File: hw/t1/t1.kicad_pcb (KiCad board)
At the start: 4 copper layers, 58 x 11.8 mm, 17 parts, among them J1 SFP_Module_Edge, J2 H-MTD PCB header (Rosenberger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, U1 DP83TG720S-Q1 / DP83TC812S-Q1, U2 STM32G031F6P6 (I2C slave: EEP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, U3 TPS62A01 3V3->1V0, Y1 25 MHz

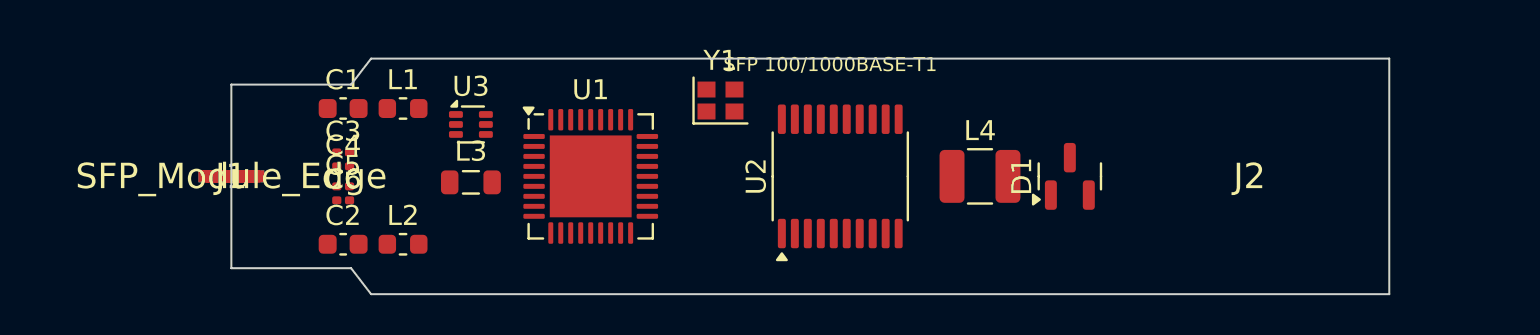
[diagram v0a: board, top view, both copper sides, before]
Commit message: T1 module: schematic, routed 4-layer PCB, fab outputs, controller firmware
One netlist in make_t1.py drives both the schematic and the PCB pad nets;
the schematic's exported netlist matches it pin for pin (175 pins), and
eeschema's ERC is clean. Every block is from its datasheet: DP83TG720S
pins, straps, MDI network and decoupling; the DP83TC812S loadout differs
only in leaving FB3 off; TPS62821 1.0 V buck.

Routed by Freerouting 1.9.0 with In1 GND / In2 3V3 planes, outer GND
pours added after import, no pour among the gold fingers. KiCad DRC:
0 violations, 0 unconnected.

Firmware (STM32G031, 1.7 KB): A0h EEPROM emulation, I2C-to-MDIO bridge at
0x56 in the mdio-i2c protocol, TX_DISABLE holds the PHY in reset, RX_LOS
follows the link.

Not orderable yet: the H-MTD footprint is a placeholder and the SGMII
widths wait on the fab's stackup.
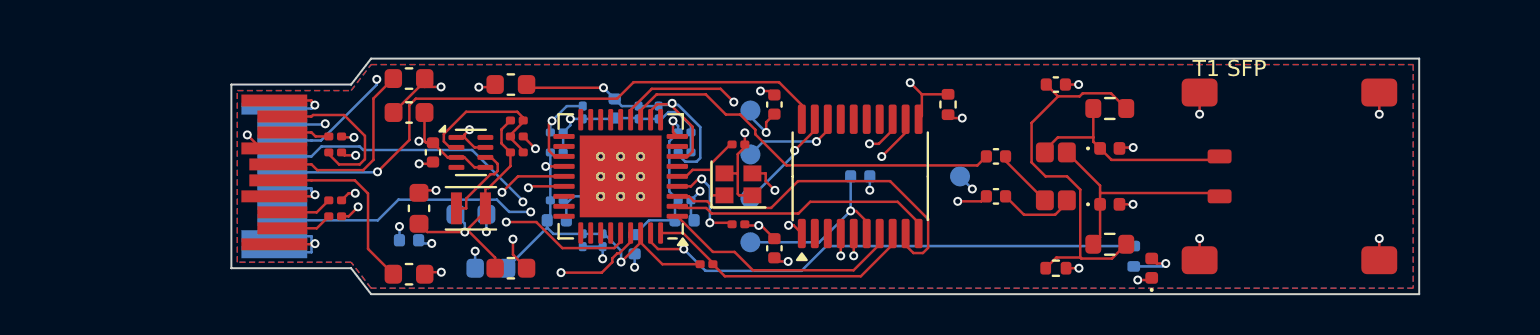
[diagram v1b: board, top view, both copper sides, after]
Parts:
- removed L3: 1uH, L_0805_2012Metric
- removed L4: CMC (ACT1210 class), L_1210_3225Metric
- added C10: 100nF, Capacitor_SMD:C_0201_0603Metric, B.Cu at (122.7, 98.8)
- added C11: 10nF, Capacitor_SMD:C_0201_0603Metric, B.Cu at (117.6, 103.2)
- added C12: 100nF, Capacitor_SMD:C_0201_0603Metric, B.Cu at (118.6, 103.2)
- added C13: 10nF, Capacitor_SMD:C_0201_0603Metric, B.Cu at (116.3, 98.8)
- added C14: 100nF, Capacitor_SMD:C_0201_0603Metric, B.Cu at (116.3, 101.2)
- added C15: 2.2uF, Capacitor_SMD:C_0402_1005Metric, B.Cu at (116.3, 102.2)
- added C16: 10nF, Capacitor_SMD:C_0201_0603Metric, B.Cu at (122.7, 97.8)
- added C17: 100nF, Capacitor_SMD:C_0201_0603Metric, B.Cu at (122.7, 101.2)
- added C18: 2.2uF, Capacitor_SMD:C_0402_1005Metric, B.Cu at (122.7, 102.2)
- added C19: 10nF, Capacitor_SMD:C_0201_0603Metric, B.Cu at (116.3, 97.8)
- added C20: 100nF, Capacitor_SMD:C_0201_0603Metric, B.Cu at (117.6, 96.8)
- added C21: 2.2uF, Capacitor_SMD:C_0402_1005Metric, B.Cu at (120.2, 103.4)
- added C24: 12pF, Capacitor_SMD:C_0201_0603Metric, F.Cu at (125.4, 98.4)
- added C25: 12pF, Capacitor_SMD:C_0201_0603Metric, F.Cu at (125.4, 102.4)
- added C26: 4.7uF, Capacitor_SMD:C_0402_1005Metric, F.Cu at (110.1, 98.8)
- added C27: 10uF, Capacitor_SMD:C_0603_1608Metric, F.Cu at (109.4, 101.6)
- added C28: 10uF, Capacitor_SMD:C_0603_1608Metric, B.Cu at (112.0, 101.9)
- added C29: 120pF, Capacitor_SMD:C_0201_0603Metric, F.Cu at (114.3, 98.8)
- added C30: 100nF, Capacitor_SMD:C_0402_1005Metric, F.Cu at (127.2, 96.4)
- added C31: 1uF, Capacitor_SMD:C_0402_1005Metric, F.Cu at (127.2, 103.6)
- added C32: 100nF, Capacitor_SMD:C_0402_1005Metric, B.Cu at (131.5, 100.0)
- added C33: 100nF 1%, Capacitor_SMD:C_0402_1005Metric, F.Cu at (138.3, 99.0)
- added C34: 100nF 1%, Capacitor_SMD:C_0402_1005Metric, F.Cu at (138.3, 101.0)
- added C35: 4.7nF, Capacitor_SMD:C_0402_1005Metric, F.Cu at (141.3, 95.4)
- added C7: 10nF, Capacitor_SMD:C_0201_0603Metric, B.Cu at (121.4, 96.8)
- added C8: 100nF, Capacitor_SMD:C_0201_0603Metric, B.Cu at (120.4, 96.8)
- added C9: 2.2uF, Capacitor_SMD:C_0402_1005Metric, B.Cu at (119.2, 96.6)
- added D2: ESD (DNP), Diode_SMD:D_0402_1005Metric, F.Cu at (144.0, 98.6)
- added D3: ESD (DNP), Diode_SMD:D_0402_1005Metric, F.Cu at (144.0, 101.4)
- added FB1: BLM18KG601SH1, Inductor_SMD:L_0603_1608Metric, F.Cu at (108.9, 95.1)
- added FB2: BLM18KG601SH1, Inductor_SMD:L_0603_1608Metric, F.Cu at (108.9, 104.9)
- added FB3: BLM18KG601SH1 (DNP for DP83TC812), Inductor_SMD:L_0603_1608Metric, F.Cu at (114.0, 104.6)
- added FB4: BLM18KG601SH1, Inductor_SMD:L_0603_1608Metric, F.Cu at (114.0, 95.4)
- added FB5: BLM18HE102SN1, Inductor_SMD:L_0603_1608Metric, B.Cu at (113.0, 104.6)
- added R1: 2.2k, Resistor_SMD:R_0201_0603Metric, F.Cu at (123.8, 104.4)
- added R2: 1k, Resistor_SMD:R_0402_1005Metric, B.Cu at (145.2, 104.0)
- added R3: 66.5k 1%, Resistor_SMD:R_0201_0603Metric, F.Cu at (114.3, 97.2)
- added R4: 100k 1%, Resistor_SMD:R_0201_0603Metric, F.Cu at (114.3, 98.0)
- added R5: 10k, Resistor_SMD:R_0402_1005Metric, F.Cu at (135.9, 96.4)
- added R6: 1k 1%, Resistor_SMD:R_0603_1608Metric, F.Cu at (144.0, 96.6)
- added R7: 1k 1%, Resistor_SMD:R_0603_1608Metric, F.Cu at (144.0, 103.4)
- added R8: 100k, Resistor_SMD:R_0402_1005Metric, F.Cu at (141.3, 104.6)
- added TP1: +3V3, TestPoint:TestPoint_Pad_D1.0mm, B.Cu at (126.0, 96.7)
- added TP2: SWDIO, TestPoint:TestPoint_Pad_D1.0mm, B.Cu at (126.0, 98.9)
- added TP3: SWCLK, TestPoint:TestPoint_Pad_D1.0mm, B.Cu at (126.0, 101.1)
- added TP4: NRST, TestPoint:TestPoint_Pad_D1.0mm, B.Cu at (126.0, 103.3)
- added TP5: GND, TestPoint:TestPoint_Pad_D1.0mm, B.Cu at (136.5, 100.0)
- C1: value 10uF VccT -> 10uF; footprint C_0603_1608Metric -> Capacitor_SMD:C_0603_1608Metric
- C2: value 10uF VccR -> 100nF; footprint C_0603_1608Metric -> Capacitor_SMD:C_0402_1005Metric; moved to B.Cu
- C3: value 100nF TD+ -> 100nF; footprint C_0201_0603Metric -> Capacitor_SMD:C_0201_0603Metric
- C4: value 100nF TD- -> 100nF; footprint C_0201_0603Metric -> Capacitor_SMD:C_0201_0603Metric
- C5: value 100nF RD+ -> 100nF; footprint C_0201_0603Metric -> Capacitor_SMD:C_0201_0603Metric
- C6: value 100nF RD- -> 100nF; footprint C_0201_0603Metric -> Capacitor_SMD:C_0201_0603Metric
- D1: value ESD, MDI -> green; footprint SOT-23 -> LED_SMD:LED_0402_1005Metric
- J1: value SFP_Module_Edge -> SFP edge (INF-8074i)
- J2: value H-MTD PCB header (Rosenberger E6A10A class) - placeholder -> H-MTD 1-port PCB header - FOOTPRINT PLACEHOLDER; footprint sfp:NOSE -> sfp:HMTD_1P_Placeholder
- L1: value ferrite VccT -> 470nH DFE201610E-R47M; footprint L_0603_1608Metric -> Inductor_SMD:L_Murata_DFE201610P
- L2: value ferrite VccR -> DLW32MH101XT2; footprint L_0603_1608Metric -> sfp:L_CommonMode_3225
- U1: value DP83TG720S-Q1 / DP83TC812S-Q1 -> DP83TG720S-Q1 (or DP83TC812S-Q1); footprint QFN-36-1EP_6x6mm_P0.5mm_EP4.1x4.1mm -> Package_DFN_QFN:QFN-36-1EP_6x6mm_P0.5mm_EP4.1x4.1mm_ThermalVias
- U2: value STM32G031F6P6 (I2C slave: EEPROM A0/A2 + MDIO bridge 0x56) -> STM32G031F6P6; footprint TSSOP-20_4.4x6.5mm_P0.65mm -> Package_SO:TSSOP-20_4.4x6.5mm_P0.65mm
- U3: value TPS62A01 3V3->1V0 -> TPS62821DLC; footprint SOT-563 -> Package_DFN_QFN:Texas_VSON-HR-8_1.5x2mm_P0.5mm
- Y1: value 25 MHz -> 25MHz CL8pF 2016; footprint Crystal_SMD_2016-4Pin_2.0x1.6mm -> Crystal:Crystal_SMD_2016-4Pin_2.0x1.6mm
- moved L2 32.9 mm to (141.3, 100.0), turned to 90 degrees
- moved D1 6.16 mm to (146.1, 104.6)
- moved L1 6.05 mm to (112.0, 101.6)
- moved Y1 4.30 mm to (125.4, 100.4)
- moved C1 3.31 mm to (108.9, 96.8)
- moved C2 3.31 mm to (108.9, 103.2)
- moved J2 2.00 mm to (153.0, 100.0)
- moved U1 1.50 mm to (119.5, 100.0), turned to 180 degrees
- moved U3 1.40 mm to (112.0, 98.8)
- moved U2 1.00 mm to (131.5, 100.0)
- moved C3 0.89 mm to (105.2, 98.0)
- moved C6 0.89 mm to (105.2, 102.0)
- moved C4 0.81 mm to (105.2, 98.8)
- moved C5 0.81 mm to (105.2, 101.2)
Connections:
- C1 pad 1: (no net) -> +3V3
- C1 pad 2: (no net) -> GND
- C2 pad 1: (no net) -> +3V3
- C2 pad 2: (no net) -> GND
- C3 pad 1: (no net) -> TD_P
- C3 pad 2: (no net) -> SG_TX_P
- C4 pad 1: (no net) -> TD_N
- C4 pad 2: (no net) -> SG_TX_N
- C5 pad 1: (no net) -> RD_P
- C5 pad 2: (no net) -> SG_RX_P
- C6 pad 1: (no net) -> RD_N
- C6 pad 2: (no net) -> SG_RX_N
- D1 pad 1: (no net) -> GND
- D1 pad 2: (no net) -> LED0_K
- J1 pad 1: (no net) -> GND
- J1 pad 10: (no net) -> GND
- J1 pad 11: (no net) -> GND
- J1 pad 12: (no net) -> RD_N
- J1 pad 13: (no net) -> RD_P
- J1 pad 14: (no net) -> GND
- J1 pad 15: (no net) -> VCCR
- J1 pad 16: (no net) -> VCCT
- J1 pad 17: (no net) -> GND
- J1 pad 18: (no net) -> TD_P
- J1 pad 19: (no net) -> TD_N
- J1 pad 2: (no net) -> TX_FAULT
- J1 pad 20: (no net) -> GND
- J1 pad 3: (no net) -> TX_DISABLE
- J1 pad 4: (no net) -> SDA
- J1 pad 5: (no net) -> SCL
- J1 pad 6: (no net) -> GND
- J1 pad 8: (no net) -> RX_LOS
- J1 pad 9: (no net) -> GND
- L1 pad 1: (no net) -> BUCK_SW
- L1 pad 2: (no net) -> V1P0_BUCK
- L2 pad 1: (no net) -> DCB_P
- L2 pad 2: (no net) -> DCB_N
- U1 pad 1: (no net) -> MDC
- U1 pad 11: (no net) -> VDDA
- U1 pad 12: (no net) -> TRD_P
- U1 pad 13: (no net) -> TRD_M
- U1 pad 2: (no net) -> PHY_INT_N
- U1 pad 21: (no net) -> VDD1P0
- U1 pad 22: (no net) -> VDDIO
- U1 pad 23: (no net) -> SG_RX_N
- U1 pad 24: (no net) -> SG_RX_P
- U1 pad 3: (no net) -> PHY_RST_N
- U1 pad 32: (no net) -> SG_TX_P
- U1 pad 33: (no net) -> SG_TX_N
- U1 pad 34: (no net) -> VDDIO
- U1 pad 35: (no net) -> LED0
- U1 pad 36: (no net) -> MDIO
- U1 pad 37: (no net) -> GND
- U1 pad 4: (no net) -> XO
- U1 pad 5: (no net) -> XI
- U1 pad 7: (no net) -> VDDA
- U1 pad 9: (no net) -> VDD1P0
- U2 pad 1: (no net) -> SDA
- U2 pad 10: (no net) -> PHY_INT_N
- U2 pad 11: (no net) -> TX_DISABLE
- U2 pad 12: (no net) -> RX_LOS
- U2 pad 13: (no net) -> TX_FAULT
- U2 pad 18: (no net) -> SWDIO
- U2 pad 19: (no net) -> SWCLK
- U2 pad 20: (no net) -> SCL
- U2 pad 4: (no net) -> +3V3
- U2 pad 5: (no net) -> GND
- U2 pad 6: (no net) -> NRST
- U2 pad 7: (no net) -> MDC
- U2 pad 8: (no net) -> MDIO
- U2 pad 9: (no net) -> PHY_RST_N
- U3 pad 1: (no net) -> +3V3
- U3 pad 2: (no net) -> BUCK_FB
- U3 pad 3: (no net) -> GND
- U3 pad 5: (no net) -> GND
- U3 pad 6: (no net) -> BUCK_SW
- Y1 pad 1: (no net) -> XI
- Y1 pad 2: (no net) -> GND
- Y1 pad 3: (no net) -> XO
- Y1 pad 4: (no net) -> GND
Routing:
- net GND: track 0.00 -> 59.5 mm, vias 0 -> 28
- net TX_DISABLE: track 0.00 -> 36.5 mm, vias 0 -> 2
- net RX_LOS: track 0.00 -> 34.2 mm, vias 0 -> 2
- net TX_FAULT: track 0.00 -> 32.3 mm, vias 0 -> 2
- net SCL: track 0.00 -> 30.1 mm, vias 0 -> 1
- net VDD1P0: track 0.00 -> 28.4 mm, vias 0 -> 3
- net SDA: track 0.00 -> 28.1 mm, vias 0 -> 2
- net LED0: track 0.00 -> 25.8 mm, vias 0 -> 1
- net TRD_M: track 0.00 -> 21.2 mm, vias 0 -> 2
- net TRD_P: track 0.00 -> 19.9 mm
- net MDI_CT: track 0.00 -> 19.5 mm
- net SG_TX_N: track 0.00 -> 18.4 mm, vias 0 -> 2
- net VDDA: track 0.00 -> 18.1 mm, vias 0 -> 2
- net VDDIO: track 0.00 -> 17.9 mm, vias 0 -> 2
- net PHY_RST_N: track 0.00 -> 17.6 mm
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- added copper zone on In2.Cu, net +3V3
- added copper zone on B.Cu, net GND
- added copper zone on F.Cu, net GND
- added copper zone on In1.Cu, net GND
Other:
- board size 58 x 11.8 mm -> 59.5 x 11.8 mm
- board text added: "T1 SFP"
- board text removed: "SFP 100/1000BASE-T1"
- board text removed: "inside cage: top <= 4.65 mm, bottom <= 1.65 mm"

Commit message: T1: orderable at JLC - real H-MTD land, JLC 3313 widths, panel, BOM/CPL with LCSC
J2 is now the Rosenberger E6S20A-40MT5-Z land from layout drawing MB_633:
ground holes 7.0 x 7.5 (9.3 is the hatched-area width, not the pitch),
signal pair 2.0 apart 1.87 behind the front row, its solder areas and
no-routing keep-outs. The body sits past the cage front, so the board
grows to 63.5 mm.

Widths from JLC04101H-3313 (50 ohm single-ended 0.157 mm); pair skew at
most 2.0 mm. TPS62822 replaces the out-of-stock TPS62821. Every assembled
part carries its LCSC number in schematic and PCB.

panel_t1.py: 5 boards, mouse bites, rails on three sides so the finger
edge stays a clean bevel edge (panel_rails.py, a KiKit framing plugin);
70.6 x 81.1 mm; panel DRC 0 errors; 265 unique placements.
Routed board: DRC 0 / unconnected 0, ERC 0.
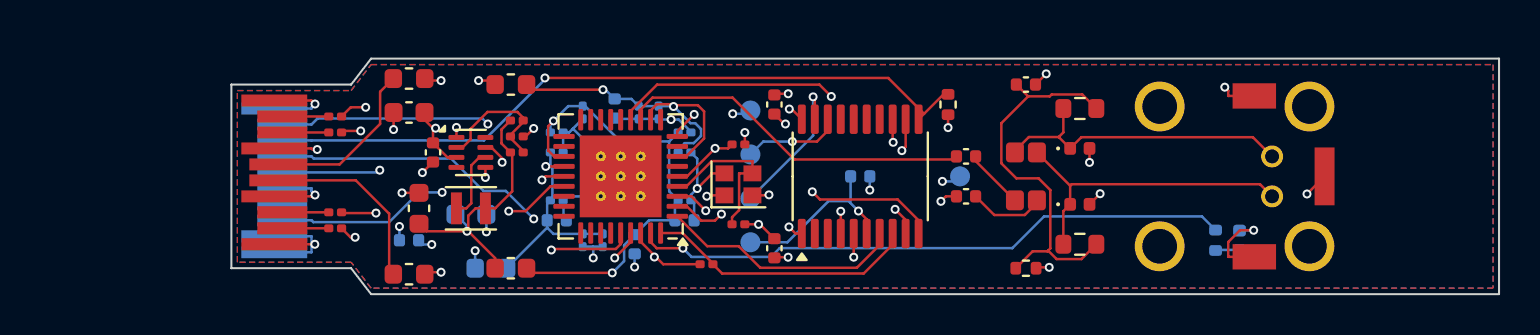
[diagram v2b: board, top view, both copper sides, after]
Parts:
- C33, C34: value 100nF 1% -> 100nF
- D1: moved to B.Cu
- J2: value H-MTD 1-port PCB header - FOOTPRINT PLACEHOLDER -> Rosenberger E6S20A-40MT5-Z (H-MTD, coding Z); footprint sfp:HMTD_1P_Placeholder -> sfp:Rosenberger_HMTD_E6S20A_1P_RA
- U3: value TPS62821DLC -> TPS62822DLC
- moved D1 4.62 mm to (150.5, 103.2), turned to -90 degrees
- moved R2 4.18 mm to (149.3, 103.2)
- moved C4 1.80 mm to (105.2, 97.0)
- moved C33 1.50 mm to (136.8, 99.0)
- moved C34 1.50 mm to (136.8, 101.0)
- moved C35 1.50 mm to (139.8, 95.4)
- moved D2 1.50 mm to (142.5, 98.6)
- moved D3 1.50 mm to (142.5, 101.4)
- moved L2 1.50 mm to (139.8, 100.0)
- moved R6 1.50 mm to (142.5, 96.6)
- moved R7 1.50 mm to (142.5, 103.4)
- moved R8 1.50 mm to (139.8, 104.6)
- moved J2 1.00 mm to (154.0, 100.0)
- moved C5 0.60 mm to (105.2, 101.8)
- moved C6 0.60 mm to (105.2, 102.6)
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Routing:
- net TD_N: track 7.99 -> 2.33 mm
- net PHY_RST_N: track 17.6 -> 13.0 mm, vias 0 -> 2
- net VDD1P0: track 28.4 -> 32.9 mm
- net LED0: track 25.8 -> 30.2 mm
- net MDI_P: track 11.2 -> 15.6 mm
- net MDI_N: track 11.5 -> 15.8 mm
- net VDDIO: track 17.9 -> 22.1 mm
- net +3V3: track 14.7 -> 11.7 mm, vias 11 -> 14
- net SCL: track 30.1 -> 27.6 mm, vias 1 -> 2
- net SWCLK: track 5.30 -> 7.54 mm
- net XO: track 10.5 -> 8.26 mm, vias 3 -> 0
- net TRD_P: track 19.9 -> 17.9 mm
- net TRD_M: track 21.2 -> 19.8 mm
- net XI: track 5.53 -> 6.88 mm, vias 0 -> 2
- net LED0_K: track 2.47 -> 1.21 mm, vias 1 -> 0
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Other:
- board size 59.5 x 11.8 mm -> 63.5 x 11.8 mm

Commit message: fw: Clause 45 over I2C (mdio-i2c framing: read 0x20|devad, write 5 bytes without it); docs: RJ45 -> RTL8221B, T1S bridge findings
The earlier docs had the C45 write frame wrong. RJ45 moves to the
RTL8221B-VB-CG (100/1000/2500, LCSC stocked; datasheet marked
confidential - noted as the one exception). T1S: no switch chip fits
(all 14x14 TQFP); CrossLink-NX SGMII exists only on csfBGA-121 and its
PCS IP is licensed; Gowin GW5AT-15 is the stocked alternative.

Also: hw/sfpgen.py is the shared generator; netclasses now really reach
the router (patterns in .kicad_pro, rewritten after every Save, routing
in a fresh process, and a guard that refuses an empty class).
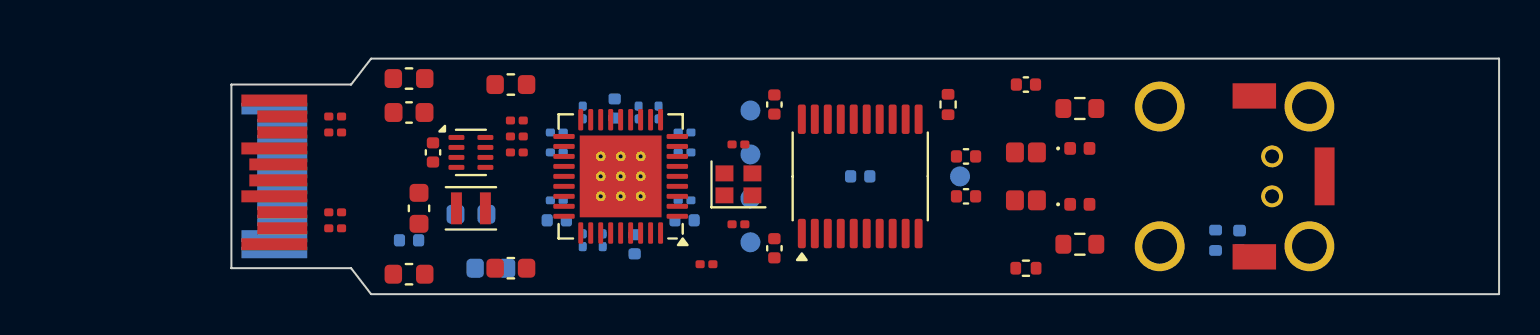
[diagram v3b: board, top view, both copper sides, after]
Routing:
- net GND: track 60.2 -> 0.00 mm, vias 28 -> 0
- net TX_DISABLE: track 36.2 -> 0.00 mm, vias 1 -> 0
- net RX_LOS: track 34.7 -> 0.00 mm, vias 2 -> 0
- net TX_FAULT: track 33.0 -> 0.00 mm, vias 2 -> 0
- net VDD1P0: track 32.9 -> 0.00 mm, vias 3 -> 0
- net LED0: track 30.2 -> 0.00 mm, vias 1 -> 0
- net SDA: track 27.9 -> 0.00 mm, vias 2 -> 0
- net SCL: track 27.6 -> 0.00 mm, vias 2 -> 0
- net VDDIO: track 22.1 -> 0.00 mm, vias 2 -> 0
- net TRD_M: track 19.8 -> 0.00 mm, vias 2 -> 0
- net MDI_CT: track 19.5 -> 0.00 mm
- net SG_TX_N: track 19.2 -> 0.00 mm, vias 2 -> 0
- net VDDA: track 18.1 -> 0.00 mm, vias 2 -> 0
- net TRD_P: track 17.9 -> 0.00 mm
- net SG_TX_P: track 17.2 -> 0.00 mm, vias 2 -> 0
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- removed copper zone on In2.Cu, net +3V3
- removed copper zone on B.Cu, net GND
- removed copper zone on F.Cu, net GND
- removed copper zone on In1.Cu, net GND

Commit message: t1: routed DRC-clean with the pairs on F/B only, panel clean
- In2's +3V3 pour goes in after routing: in the DSN it made +3V3 a plane
  net the router never routed, while signals cut the plane up
- SGMII/MDI classes restricted to F and B (use_layer): the router had
  split pairs P-on-B / N-on-In2. U1 pins 12/13 cross over on purpose;
  the PHY corrects MDI polarity itself (datasheet 6.4.7.2)
- placement: Y1 turned 180 so XI/XO face pins 5/4 uncrossed, load caps
  underneath; buck rearranged (divider by FB, input cap under VIN, EN to
  VIN under the package); SWD test points moved off the crystal
- locked pre-routes and escape vias where the router kept failing,
  cap dogbones, then post-route repair: unused escape vias out, open
  links joined before GND stitching, vias into ground islands
- panel: mouse bites 0.1 mm into the board, stitching 1 mm off the long
  edges, bottom label off the edge; panel DRC 0 errors
- ERC 0/0, DRC 0 violations 0 unconnected, pair skew <= 3.2 mm
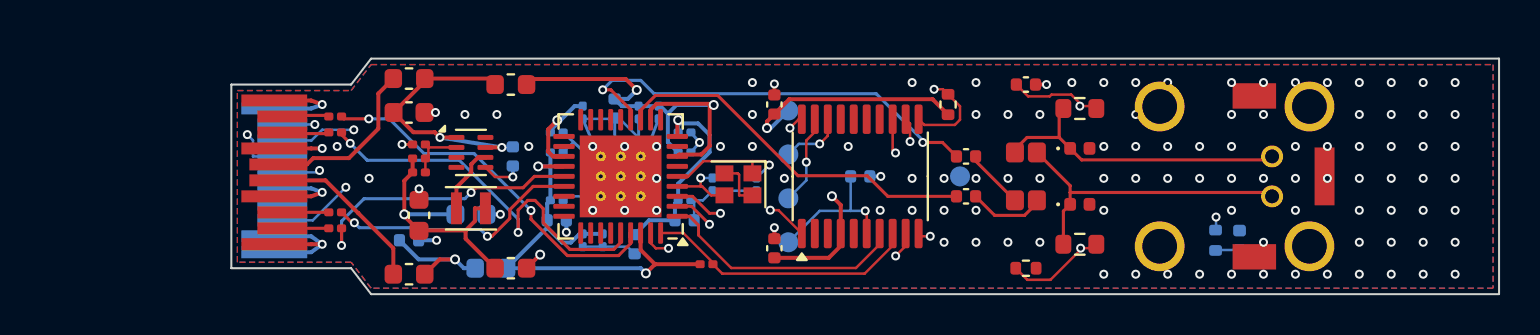
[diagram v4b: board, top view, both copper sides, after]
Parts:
- C24, C25, C26: moved to B.Cu
- moved R3 5.55 mm to (109.4, 99.8)
- moved R4 4.92 mm to (109.4, 98.4), turned to 180 degrees
- moved C29 4.91 mm to (109.4, 99.1)
- moved C26 4.00 mm to (114.1, 99.0), turned to -90 degrees
- moved C25 2.39 mm to (124.1, 100.4), turned to -90 degrees
- moved C24 2.19 mm to (126.3, 100.4), turned to -90 degrees
- moved TP1 1.90 mm to (127.9, 96.7)
- moved TP2 1.90 mm to (127.9, 98.9)
- moved TP3 1.90 mm to (127.9, 101.1)
- moved TP4 1.90 mm to (127.9, 103.3)
- moved C27 0.35 mm to (109.4, 102.0)
- turned Y1 to 180 degrees
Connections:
- U1 pad 12: TRD_P -> TRD_M
- U1 pad 13: TRD_M -> TRD_P
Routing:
- net +3V3: track 0.00 -> 64.0 mm, vias 0 -> 5
- net GND: track 0.00 -> 56.3 mm, vias 0 -> 118
- net TX_FAULT: track 0.00 -> 41.2 mm, vias 0 -> 2
- net TX_DISABLE: track 0.00 -> 39.1 mm, vias 0 -> 2
- net RX_LOS: track 0.00 -> 38.4 mm, vias 0 -> 2
- net SDA: track 0.00 -> 35.8 mm, vias 0 -> 2
- net LED0: track 0.00 -> 31.3 mm, vias 0 -> 2
- net VDD1P0: track 0.00 -> 29.7 mm, vias 0 -> 3
- net SCL: track 0.00 -> 28.5 mm, vias 0 -> 2
- net VDDIO: track 0.00 -> 23.7 mm, vias 0 -> 2
- net VDDA: track 0.00 -> 22.5 mm, vias 0 -> 2
- net TRD_P: track 0.00 -> 21.9 mm, vias 0 -> 2
- net SG_TX_P: track 0.00 -> 19.9 mm, vias 0 -> 2
- net TRD_M: track 0.00 -> 18.7 mm
- net SG_TX_N: track 0.00 -> 18.4 mm, vias 0 -> 2
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- added copper zone on In2.Cu, net +3V3
- added copper zone on B.Cu, net GND
- added copper zone on F.Cu, net GND
- added copper zone on In1.Cu, net GND

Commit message: t1: opens clean in KiCad 9 - schematic parity, linked footprints, check script
A KiCad 9 check (official Docker image, as a reviewer would open it) found
what KiCad 7's python and kicad-cli could not test:
- no footprint was linked to its schematic symbol: KiCad's Update PCB
  would have replaced every part. Footprints now carry /<symbol uuid>
  plus Sheetname/Sheetfile
- 140 net-name conflicts: local labels name nets /TD_P on the root sheet,
  the board says TD_P. The schematic now uses global labels
- no-connect pins are nets of their own in KiCad
  (unconnected-(REF-PIN-PadN)); the pads now carry them
- DNP/BOM flags agreed nowhere (ESD diodes, test pads): excluded from the
  BOM on both sides (KiCad 7 boards have no DNP attribute)
- back-side label was not mirrored
- the buck's footprint is gone from KiCad 9's library: vendored into
  hw/fp/sfp.pretty

Result (sh hw/check_kicad9.sh t1): DRC 0 errors / 0 unconnected, parity
clean, ERC 0 errors; the only warnings are KiCad 9's newer library copies.
Copper is unchanged (tracks, vias, pads and fills compared item by item);
gerber/CPL/BOM changes are ordering only. KiCad 7 ERC 0/0, DRC 0/0.
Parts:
- U3: footprint Package_DFN_QFN:Texas_VSON-HR-8_1.5x2mm_P0.5mm -> sfp:Texas_VSON-HR-8_1.5x2mm_P0.5mm
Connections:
- J1 pad 7: (no net) -> unconnected-(J1-RS0-Pad7)
- U1 pad 10: (no net) -> unconnected-(U1-INH-Pad10)
- U1 pad 14: (no net) -> unconnected-(U1-STRP_1-Pad14)
- U1 pad 15: (no net) -> unconnected-(U1-RX_CTRL-Pad15)
- U1 pad 16: (no net) -> unconnected-(U1-CLKOUT-Pad16)
- U1 pad 17: (no net) -> unconnected-(U1-DNC-Pad17)
- U1 pad 18: (no net) -> unconnected-(U1-DNC-Pad18)
- U1 pad 19: (no net) -> unconnected-(U1-DNC-Pad19)
- U1 pad 20: (no net) -> unconnected-(U1-DNC-Pad20)
- U1 pad 25: (no net) -> unconnected-(U1-RX_D1-Pad25)
- U1 pad 26: (no net) -> unconnected-(U1-RX_D0-Pad26)
- U1 pad 27: (no net) -> unconnected-(U1-RX_CLK-Pad27)
- U1 pad 28: (no net) -> unconnected-(U1-TX_CLK-Pad28)
- U1 pad 29: (no net) -> unconnected-(U1-TX_CTRL-Pad29)
- U1 pad 30: (no net) -> unconnected-(U1-TX_D3-Pad30)
- U1 pad 31: (no net) -> unconnected-(U1-TX_D2-Pad31)
- U1 pad 6: (no net) -> unconnected-(U1-LED_1/AUTO-Pad6)
- U1 pad 8: (no net) -> unconnected-(U1-WAKE-Pad8)
- U2 pad 14: (no net) -> unconnected-(U2-PA7-Pad14)
- U2 pad 15: (no net) -> unconnected-(U2-PB0/PB1/PB2/PA8-Pad15)
- U2 pad 16: (no net) -> unconnected-(U2-PA11/PA9-Pad16)
- U2 pad 17: (no net) -> unconnected-(U2-PA12/PA10-Pad17)
- U2 pad 2: (no net) -> unconnected-(U2-PC14/PB9-Pad2)
- U2 pad 3: (no net) -> unconnected-(U2-PC15-Pad3)
- U3 pad 4: (no net) -> unconnected-(U3-NC-Pad4)
- U3 pad 8: (no net) -> unconnected-(U3-PG-Pad8)
